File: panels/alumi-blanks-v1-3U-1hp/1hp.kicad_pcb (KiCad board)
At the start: 2 copper layers, 5 x 128.5 mm, 2 parts

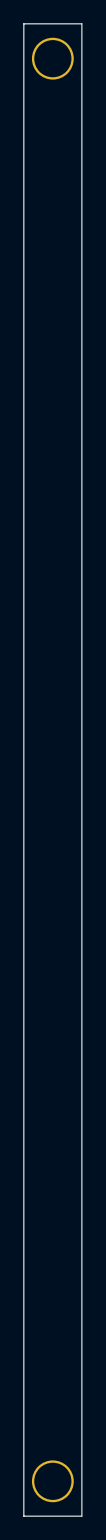
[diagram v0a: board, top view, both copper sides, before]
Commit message: feat: add new screw hole footprints and update panel KiCad files for new JLCPCB order
- Added modular-3M-screw-hole-size1-alumi-0604, modular-3M-screw-hole-size1-fit-alumi-0604, modular-3M-screw-hole-size2-alumi-0604
- Updated all panel .kicad_pcb and .kicad_pro files for 3U panels (1hp-16hp)
- Added new JLCPCB order snapshot and Gerber outputs

Co-authored-by: Copilot <223556219+Copilot@users.noreply.github.com>
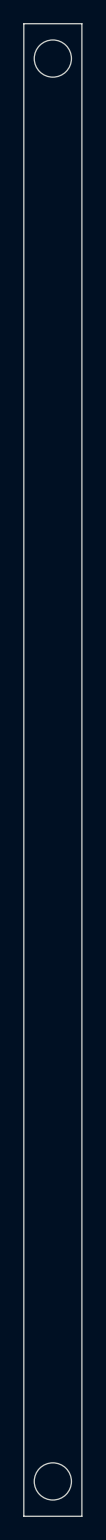
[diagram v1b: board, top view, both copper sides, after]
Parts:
- removed the REF** at (2.50, 125.5)
- removed the REF** at (2.50, 3.01)
- added REF**: modular-3M-screw-hole-size1-fit-alumi-0604, zudo-blanks:modular-3M-screw-hole-size1-fit-alumi-0604, F.Cu at (2.50, 125.5)
- added REF**: modular-3M-screw-hole-size1-fit-alumi-0604, zudo-blanks:modular-3M-screw-hole-size1-fit-alumi-0604, F.Cu at (2.50, 3.00)
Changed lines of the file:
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@@
 (kicad_pcb
-	(version 20240108)
+	(version 20260206)
 	(generator "pcbnew")
-	(generator_version "8.0")
+	(generator_version "10.0")
 	(general
 		(thickness 1.6)
@@
 	(layers
 		(0 "F.Cu" signal)
-		(31 "B.Cu" signal)
-		(32 "B.Adhes" user "B.Adhesive")
-		(33 "F.Adhes" user "F.Adhesive")
-		(34 "B.Paste" user)
-		(35 "F.Paste" user)
-		(36 "B.SilkS" user "B.Silkscreen")
-		(37 "F.SilkS" user "F.Silkscreen")
-		(38 "B.Mask" user)
-		(39 "F.Mask" user)
-		(40 "Dwgs.User" user "User.Drawings")
-		(41 "Cmts.User" user "User.Comments")
-		(42 "Eco1.User" user "User.Eco1")
-		(43 "Eco2.User" user "User.Eco2")
-		(44 "Edge.Cuts" user)
-		(45 "Margin" user)
-		(46 "B.CrtYd" user "B.Courtyard")
-		(47 "F.CrtYd" user "F.Courtyard")
-		(48 "B.Fab" user)
-		(49 "F.Fab" user)
-		(50 "User.1" user)
-		(51 "User.2" user)
-		(52 "User.3" user)
-		(53 "User.4" user)
-		(54 "User.5" user)
-		(55 "User.6" user)
-		(56 "User.7" user)
-		(57 "User.8" user)
-		(58 "User.9" user)
+		(2 "B.Cu" signal)
+		(9 "F.Adhes" user "F.Adhesive")
+		(11 "B.Adhes" user "B.Adhesive")
+		(13 "F.Paste" user)
+		(15 "B.Paste" user)
+		(5 "F.SilkS" user "F.Silkscreen")
+		(7 "B.SilkS" user "B.Silkscreen")
+		(1 "F.Mask" user)
+		(3 "B.Mask" user)
+		(17 "Dwgs.User" user "User.Drawings")
+		(19 "Cmts.User" user "User.Comments")
+		(21 "Eco1.User" user "User.Eco1")
+		(23 "Eco2.User" user "User.Eco2")
+		(25 "Edge.Cuts" user)
+		(27 "Margin" user)
+		(31 "F.CrtYd" user "F.Courtyard")
+		(29 "B.CrtYd" user "B.Courtyard")
+		(35 "F.Fab" user)
+		(33 "B.Fab" user)
+		(39 "User.1" user)
+		(41 "User.2" user)
+		(43 "User.3" user)
+		(45 "User.4" user)
+		(47 "User.5" user)
+		(49 "User.6" user)
+		(51 "User.7" user)
+		(53 "User.8" user)
+		(55 "User.9" user)
 	)
 	(setup
 		(pad_to_mask_clearance 0)
 		(allow_soldermask_bridges_in_footprints no)
+		(tenting
+			(front yes)
+			(back yes)
+		)
+		(covering
+			(front no)
+			(back no)
+		)
+		(plugging
+			(front no)
+			(back no)
+		)
+		(capping no)
+		(filling no)
 		(pcbplotparams
-			(layerselection 0x00010fc_ffffffff)
-			(plot_on_all_layers_selection 0x0000000_00000000)
+			(layerselection 0x00000000_00000000_55555555_5755555a)
+			(plot_on_all_layers_selection 0x00000000_00000000_00000000_00000000)
 			(disableapertmacros no)
 			(usegerberextensions no)
@@
 			(usegerberadvancedattributes yes)
 			(creategerberjobfile yes)
-			(dashed_line_dash_ratio 12.000000)
-			(dashed_line_gap_ratio 3.000000)
+			(dashed_line_dash_ratio 12)
+			(dashed_line_gap_ratio 3)
 			(svgprecision 4)
 			(plotframeref no)
-			(viasonmask no)
 			(mode 1)
 			(useauxorigin no)
-			(hpglpennumber 1)
-			(hpglpenspeed 20)
-			(hpglpendiameter 15.000000)
 			(pdf_front_fp_property_popups yes)
 			(pdf_back_fp_property_popups yes)
+			(pdf_metadata yes)
+			(pdf_single_document no)
 			(dxfpolygonmode yes)
-			(dxfimperialunits yes)
+			(dxfimperialunits no)
 			(dxfusepcbnewfont yes)
 			(psnegative no)
 			(psa4output no)
-			(plotreference yes)
-			(plotvalue yes)
-			(plotfptext yes)
-			(plotinvisibletext no)
+			(plot_black_and_white yes)
 			(sketchpadsonfab no)
+			(plotpadnumbers no)
+			(hidednponfab no)
+			(sketchdnponfab yes)
+			(crossoutdnponfab yes)
 			(subtractmaskfromsilk no)
 			(outputformat 1)
@@
 		)
 	)
-	(net 0 "")
-	(footprint "Takazudo:M3-hole-deco"
+	(footprint "zudo-blanks:modular-3M-screw-hole-size1-fit-alumi-0604"
 		(layer "F.Cu")
-		(at 2.5 125.49)
+		(at 2.5 125.5)
 		(property "Reference" "REF**"
 			(at 0 -0.5 0)
@@
 			)
 		)
-		(property "Value" "M3-hole-deco"
+		(property "Value" "modular-3M-screw-hole-size1-fit-alumi-0604"
 			(at 0 1 0)
 			(unlocked yes)
@@
 			)
 		)
-		(property "Footprint" "Takazudo:M3-hole-deco"
-			(at 0 0 0)
-			(unlocked yes)
-			(layer "F.Fab")
-			(hide yes)
-			(effects
-				(font
-					(size 1 1)
-					(thickness 0.15)
-				)
-			)
-		)
 		(property "Datasheet" ""
 			(at 0 0 0)
@@
 			)
 		)
-		(attr through_hole)
-		(pad "1" thru_hole roundrect
+		(attr smd)
+		(duplicate_pad_numbers_are_jumpers no)
+		(pad "" np_thru_hole roundrect
 			(at 0 0 90)
-			(size 3.6 3.6)
-			(drill 3.2)
-			(layers "*.Cu" "*.Mask")
-			(remove_unused_layers no)
-			(roundrect_rratio 0.5)
-		)
-	)
-	(footprint "Takazudo:M3-hole-deco"
+			(size 4 4)
+			(drill oval 3.2)
+			(layers "*.Mask")
+			(roundrect_rratio 0.4998750312)
+		)
+		(embedded_fonts no)
+	)
+	(footprint "zudo-blanks:modular-3M-screw-hole-size1-fit-alumi-0604"
 		(layer "F.Cu")
-		(at 2.5 3.01)
+		(at 2.5 3)
 		(property "Reference" "REF**"
 			(at 0 -0.5 0)
@@
 			)
 		)
-		(property "Value" "M3-hole-deco"
+		(property "Value" "modular-3M-screw-hole-size1-fit-alumi-0604"
 			(at 0 1 0)
 			(unlocked yes)
@@
 			)
 		)
-		(property "Footprint" "Takazudo:M3-hole-deco"
-			(at 0 0 0)
-			(unlocked yes)
-			(layer "F.Fab")
-			(hide yes)
-			(effects
-				(font
-					(size 1 1)
-					(thickness 0.15)
-				)
-			)
-		)
 		(property "Datasheet" ""
 			(at 0 0 0)
@@
 			)
 		)
-		(attr through_hole)
-		(pad "1" thru_hole roundrect
+		(attr smd)
+		(duplicate_pad_numbers_are_jumpers no)
+		(pad "" np_thru_hole roundrect
 			(at 0 0 90)
-			(size 3.6 3.6)
-			(drill 3.2)
-			(layers "*.Cu" "*.Mask")
-			(remove_unused_layers no)
-			(roundrect_rratio 0.5)
-		)
-	)
-	(gr_poly
-		(pts
-			(xy 4.998236 128.491608) (xy 0 128.491608) (xy 0 0.008385) (xy 4.998236 0.008385)
-		)
-		(stroke
-			(width 0.1)
-			(type solid)
-		)
-		(fill solid)
+			(size 4 4)
+			(drill oval 3.2)
+			(layers "*.Mask")
+			(roundrect_rratio 0.4998750312)
+		)
+		(embedded_fonts no)
+	)
+	(gr_rect
+		(start 0 0)
+		(end 5 128.5)
+		(stroke
+			(width 0.05)
+			(type solid)
+		)
+		(fill no)
 		(layer "Edge.Cuts")
 	)
@@
 			(type solid)
 		)
-		(fill solid)
+		(fill yes)
 		(layer "User.1")
 	)
@@
 			(type solid)
 		)
-		(fill solid)
+		(fill yes)
 		(layer "User.1")
 	)
@@
 			(type solid)
 		)
-		(fill solid)
+		(fill yes)
+		(layer "User.1")
+	)
+	(gr_poly
+		(pts
+			(xy 4.998227 128.491623) (xy 4.299815 128.491623) (xy 4.299812 98.495155) (xy 4.998225 98.495155)
+		)
+		(stroke
+			(width -0.000001)
+			(type solid)
+		)
+		(fill yes)
+		(layer "User.1")
+	)
+	(gr_poly
+		(pts
+			(xy 4.998236 30.004854) (xy 4.299823 30.004854) (xy 4.299823 0.008385) (xy 4.998236 0.008385)
+		)
+		(stroke
+			(width -0.000001)
+			(type solid)
+		)
+		(fill yes)
 		(layer "User.1")
 	)
@@
 			(type solid)
 		)
-		(fill solid)
-		(layer "User.1")
-	)
-	(gr_poly
-		(pts
-			(xy 4.998227 128.491623) (xy 4.299815 128.491623) (xy 4.299812 98.495155) (xy 4.998225 98.495155)
-		)
-		(stroke
-			(width -0.000001)
-			(type solid)
-		)
-		(fill solid)
-		(layer "User.1")
-	)
-	(gr_poly
-		(pts
-			(xy 4.998236 30.004854) (xy 4.299823 30.004854) (xy 4.299823 0.008385) (xy 4.998236 0.008385)
-		)
-		(stroke
-			(width -0.000001)
-			(type solid)
-		)
-		(fill solid)
-		(layer "User.1")
-	)
+		(fill yes)
+		(layer "User.1")
+	)
+	(embedded_fonts no)
 )
